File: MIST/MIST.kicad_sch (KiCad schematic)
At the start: 2 parts

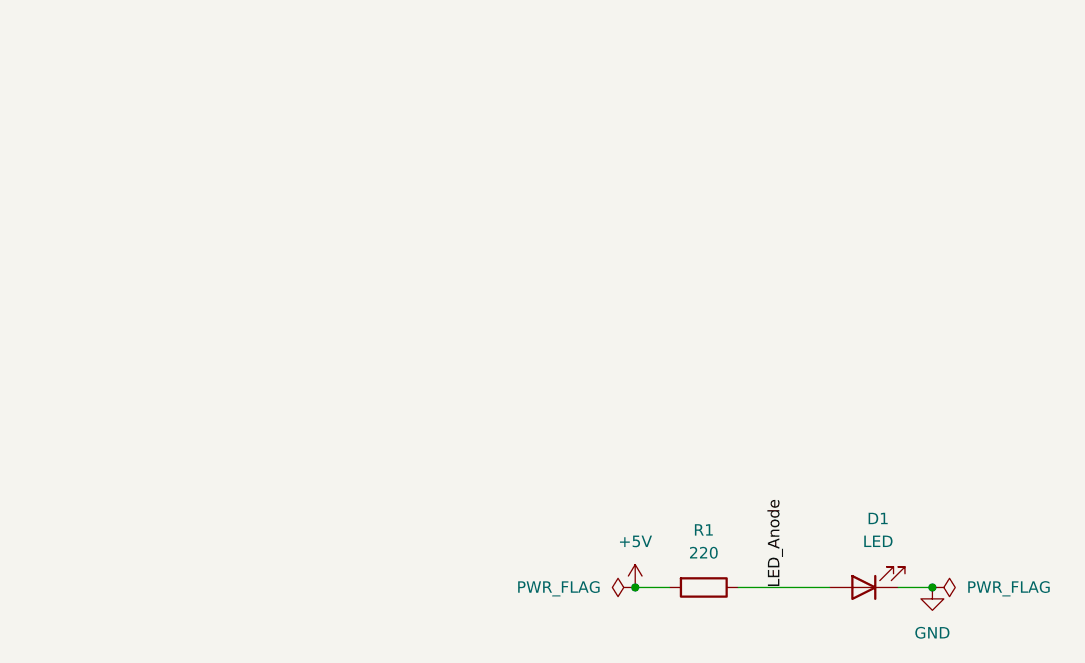
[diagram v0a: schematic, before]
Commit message: finished BOM and added resources and started layout
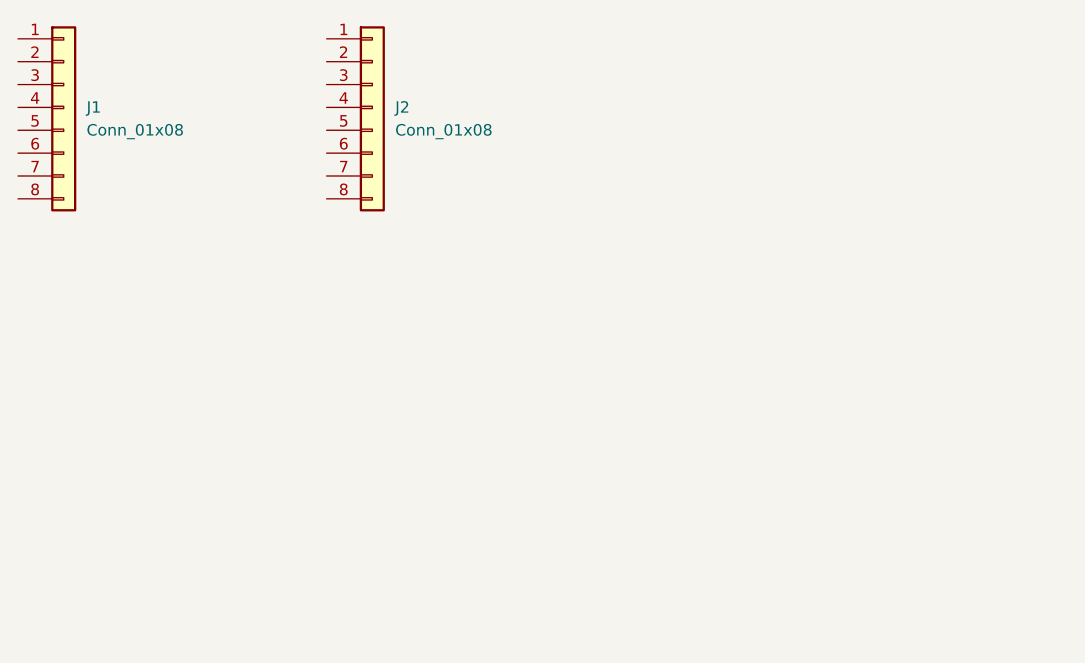
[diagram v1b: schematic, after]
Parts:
- removed D1: LED, LED_SMD:LED-APA102-2020, symbol Device:LED
- removed R1: 220, Resistor_SMD:R_0201_0603Metric, symbol Device:R
- added J1, J2: Conn_01x08, Connector_PinHeader_2.54mm:PinHeader_1x08_P2.54mm_Vertical, symbol Connector_Generic:Conn_01x08

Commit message: finished schematic. updated BOM. stuff.
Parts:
- added C1, C2: 100n, Capacitor_SMD:C_0805_2012Metric, symbol Device:C
- added C3, C4: 22pF, Capacitor_SMD:C_0805_2012Metric, symbol Device:C
- added C5: 22uF, Capacitor_SMD:C_0805_2012Metric, symbol Device:C
- added C6, C8, C9: 0.1u, symbol Device:C
- added C7: 0.1n, symbol Device:C
- added J3: USB_C_Receptacle_PowerOnly_6P, Connector_USB:USB_C_Receptacle_GCT_USB4125-xx-x_6P_TopMnt_Horizontal, symbol Connector:USB_C_Receptacle_PowerOnly_6P
- added J4: ICSP, Connector_PinHeader_2.54mm:PinHeader_2x03_P2.54mm_Vertical, symbol Connector_Generic:Conn_02x03_Odd_Even
- added MK1: CMC-5042PF-AC, CMC-5042PF-AC:CUI_CMC-5042PF-AC, symbol CMC-5042PF-AC:CMC-5042PF-AC
- added R1: 10k, Resistor_SMD:R_1206_3216Metric, symbol Device:R
- added R10: 100k, symbol Device:R
- added R2, R3: 10k, symbol Device:R
- added R4, R5: 5.1k, Resistor_SMD:R_1206_3216Metric, symbol Device:R
- added R6, R7: 2k, symbol Device:R
- added R8, R9: 1M, symbol Device:R
- added S1, S2: SKRPABE010, SKRPABE010:SW_SKRPABE010, symbol SKRPABE010:SKRPABE010
- added U1: ATmega328PB-A, Package_QFP:TQFP-32_7x7mm_P0.8mm, symbol MCU_Microchip_ATmega:ATmega328PB-A
- added U2: MAX7219, symbol Driver_LED:MAX7219
- added U3: MAX4466EXK, MAX4466EXK:SOT65P210X110-5N, symbol MAX4466EXK:MAX4466EXK
- added Y1: 16 Mhz Crystal, Crystal:Crystal_SMD_3225-4Pin_3.2x2.5mm, symbol Device:Crystal_GND24
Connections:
- net ROW1 (P9): now reaches J2.1 (Pin_1)
- net ROW1 (P9): now also U2.2 (DIG_0)
- net ROW2 (P14): now reaches J2.2 (Pin_2)
- net ROW2 (P14): now also U2.11 (DIG_1)
- net ROW3 (P8): now reaches J2.3 (Pin_3)
- net ROW3 (P8): now also U2.6 (DIG_2)
- net ROW4 (P12): now reaches J2.4 (Pin_4)
- net ROW4 (P12): now also U2.7 (DIG_3)
- net ROW5 (P1): now reaches J2.5 (Pin_5)
- net ROW5 (P1): now also U2.3 (DIG_4)
- net ROW6 (P7): now reaches J2.6 (Pin_6)
- net ROW6 (P7): now also U2.10 (DIG_5)
- net ROW7 (P2): now reaches J2.7 (Pin_7)
- net ROW7 (P2): now also U2.5 (DIG_6)
- net ROW8 (P5): now reaches J2.8 (Pin_8)
- net ROW8 (P5): now also U2.8 (DIG_7)
- net COL1 (P13): now reaches J1.1 (Pin_1)
- net COL1 (P13): now also U2.22 (SEG_DP)
- net COL2 (P3): now reaches J1.2 (Pin_2)
- net COL2 (P3): now also U2.14 (SEG_A)
- net COL3 (P4): now reaches J1.3 (Pin_3)
- net COL3 (P4): now also U2.16 (SEG_B)
- net COL4 (P10): now reaches J1.4 (Pin_4)
- net COL4 (P10): now also U2.20 (SEG_C)
- net COL5 (P6): now reaches J1.5 (Pin_5)
- net COL5 (P6): now also U2.23 (SEG_D)
- net COL6 (P11): now reaches J1.6 (Pin_6)
- net COL6 (P11): now also U2.21 (SEG_E)
- net COL7 (P15): now reaches J1.7 (Pin_7)
- net COL7 (P15): now also U2.15 (SEG_F)
- net COL8 (P16): now reaches J1.8 (Pin_8)
- net COL8 (P16): now also U2.17 (SEG_G)
- new net: C6.2, R6.2, R7.1
- new net: MK1.OUT, R7.2, R8.2, R9.1, U3.1 (IN+)
- new net: R3.1, U2.18 (ISET)
- new net: C7.1, R10.1, R2.1, U3.3 (IN-)
- new net !RESET: J4.5 (Pin_5), R1.1, S1.1, S1.2, U1.29 (~{RESET}/PC6)
- new net +5V: C1.2, C5.2, C8.1, C9.1, J3.A9 (VBUS), J3.B9 (VBUS), J4.2 (Pin_2), R1.2, R3.2, R6.1, R8.1, U1.18 (AVCC), U1.4 (VCC), U2.19 (V+), U3.5 (VCC)
- new net ADC0: C7.2, R10.2, U1.23 (PC0), U3.4 (OUT)
- new net AREF: C2.2, U1.20 (AREF)
- new net CC1: J3.A5 (CC1), R5.1
- new net CC2: J3.B5 (CC2), R4.1
- new net GND: C1.1, C2.1, C3.2, C4.1, C5.1, C6.1, C8.2, C9.2, J3.A12 (GND), J3.B12 (GND), J3.S1 (SHIELD), J4.6 (Pin_6), MK1.GND, R2.2, R4.2, R5.2, R9.2, S1.3, S1.4, S2.3, S2.4, U1.21 (GND), U1.5 (GND), U2.4 (GND), U2.9 (GND), U3.2 (GND), Y1.2, Y1.4
- new net MISO: J4.1 (Pin_1), U1.16 (PB4)
- new net MOSI: J4.4 (Pin_4), U1.15 (PB3), U2.1 (DIN)
- new net SCK: J4.3 (Pin_3), U1.17 (PB5), U2.13 (CLK)
- new net SS: U1.14 (PB2), U2.12 (LOAD)
- new net SWITCHMODE: S2.1, S2.2, U1.2 (PD4)
- new net XTAL1: C3.1, U1.7 (XTAL1/PB6), Y1.1
- new net XTAL2: C4.2, U1.8 (XTAL2/PB7), Y1.3
- no-connect marks 0 -> 19
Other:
- note added: "Bulk Capacitor"
- note added: "Crystal Oscillator"
- note added: "In-Circuit Serial Programming"
- note added: "LED Matrix"
- note added: "Microcontroller"
- note added: "Microphone"
- note added: "Reset Button"
- note added: "Switch Mode Button"
- note added: "USB Type-C - Power Only"
- moved on the sheet: J1, J2

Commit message: finished schematic and layout
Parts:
- C6, C7, C8, C9, R3: footprint (none) -> Capacitor_SMD:C_0805_2012Metric
- R10, R2, R6, R7, R8, R9: footprint (none) -> Resistor_SMD:R_0805_2012Metric
- R4, R5: footprint Resistor_SMD:R_1206_3216Metric -> Capacitor_SMD:C_0805_2012Metric
- U2: footprint (none) -> Package_SO:SOIC-24W_7.5x15.4mm_P1.27mm
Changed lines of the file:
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@@
 			)
 		)
-		(property "Footprint" ""
+		(property "Footprint" "Capacitor_SMD:C_0805_2012Metric"
 			(at 266.7 48.5648 0)
 			(effects
@@
 			)
 		)
-		(property "Footprint" "Resistor_SMD:R_1206_3216Metric"
+		(property "Footprint" "Capacitor_SMD:C_0805_2012Metric"
 			(at 87.122 166.37 90)
 			(effects
@@
 			)
 		)
-		(property "Footprint" ""
+		(property "Footprint" "Resistor_SMD:R_0805_2012Metric"
 			(at 289.052 55.88 90)
 			(effects
@@
 			)
 		)
-		(property "Footprint" ""
+		(property "Footprint" "Capacitor_SMD:C_0805_2012Metric"
 			(at 269.748 127 90)
 			(effects
@@
 			)
 		)
-		(property "Footprint" ""
+		(property "Footprint" "Package_SO:SOIC-24W_7.5x15.4mm_P1.27mm"
 			(at 281.94 149.86 0)
 			(effects
@@
 			)
 		)
-		(property "Footprint" "Resistor_SMD:R_1206_3216Metric"
+		(property "Footprint" "Capacitor_SMD:C_0805_2012Metric"
 			(at 97.282 166.37 90)
 			(effects
@@
 			)
 		)
-		(property "Footprint" ""
+		(property "Footprint" "Resistor_SMD:R_0805_2012Metric"
 			(at 337.82 94.488 90)
 			(effects
@@
 			)
 		)
-		(property "Footprint" ""
+		(property "Footprint" "Capacitor_SMD:C_0805_2012Metric"
 			(at 341.63 105.7148 0)
 			(effects
@@
 			)
 		)
-		(property "Footprint" ""
+		(property "Footprint" "Capacitor_SMD:C_0805_2012Metric"
 			(at 263.8552 151.13 0)
 			(effects
@@
 			)
 		)
-		(property "Footprint" ""
+		(property "Footprint" "Resistor_SMD:R_0805_2012Metric"
 			(at 273.812 55.88 90)
 			(effects
@@
 			)
 		)
-		(property "Footprint" ""
+		(property "Footprint" "Resistor_SMD:R_0805_2012Metric"
 			(at 289.052 78.74 90)
 			(effects
@@
 			)
 		)
-		(property "Footprint" ""
+		(property "Footprint" "Resistor_SMD:R_0805_2012Metric"
 			(at 273.812 43.18 90)
 			(effects
@@
 			)
 		)
-		(property "Footprint" ""
+		(property "Footprint" "Resistor_SMD:R_0805_2012Metric"
 			(at 303.022 78.74 90)
 			(effects
@@
 			)
 		)
-		(property "Footprint" ""
+		(property "Footprint" "Capacitor_SMD:C_0805_2012Metric"
 			(at 371.8052 46.99 0)
 			(effects

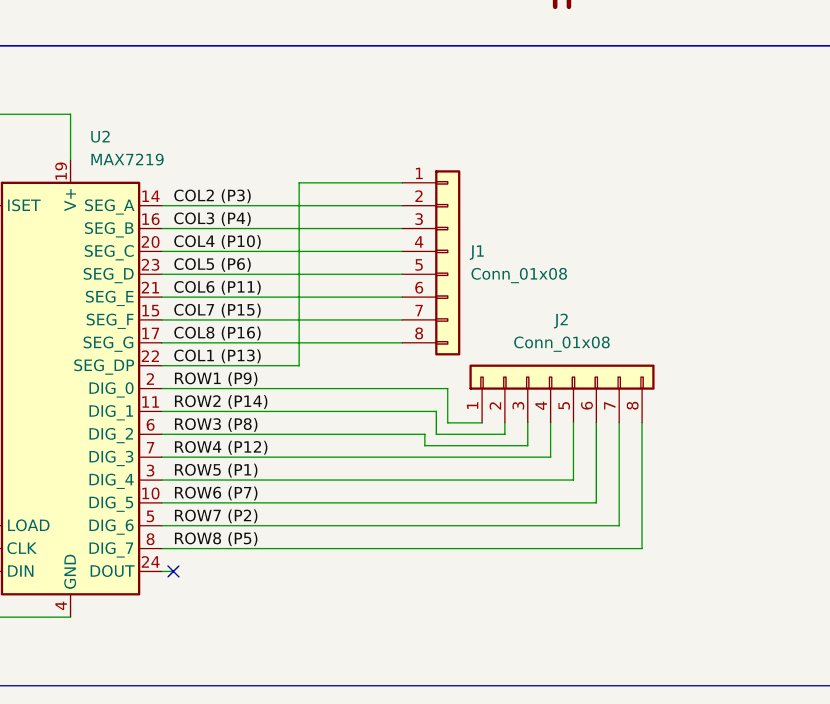
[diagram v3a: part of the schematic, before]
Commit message: fixed wrong matrix pin mappings schematic.
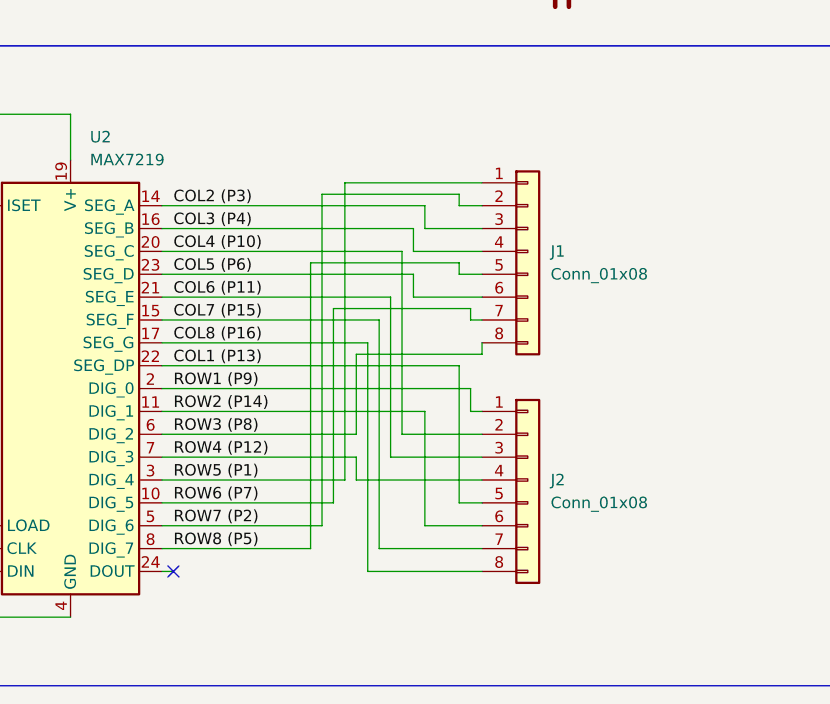
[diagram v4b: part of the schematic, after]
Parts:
- R1: footprint Resistor_SMD:R_1206_3216Metric -> Resistor_SMD:R_0805_2012Metric
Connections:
- net COL1 (P13): now also J2.5 (Pin_5); no longer J1.1 (Pin_1)
- net COL2 (P3): now also J1.3 (Pin_3); no longer J1.2 (Pin_2)
- net COL3 (P4): now also J1.4 (Pin_4); no longer J1.3 (Pin_3)
- net COL4 (P10): now also J2.2 (Pin_2); no longer J1.4 (Pin_4)
- net COL5 (P6): now also J1.6 (Pin_6); no longer J1.5 (Pin_5)
- net COL6 (P11): now also J2.3 (Pin_3); no longer J1.6 (Pin_6)
- net COL7 (P15): now also J2.7 (Pin_7); no longer J1.7 (Pin_7)
- net COL8 (P16): now also J2.8 (Pin_8); no longer J1.8 (Pin_8)
- net ROW2 (P14): now also J2.6 (Pin_6); no longer J2.2 (Pin_2)
- net ROW3 (P8): now also J1.8 (Pin_8); no longer J2.3 (Pin_3)
- net ROW5 (P1): now also J1.1 (Pin_1); no longer J2.5 (Pin_5)
- net ROW6 (P7): now also J1.7 (Pin_7); no longer J2.6 (Pin_6)
- net ROW7 (P2): now also J1.2 (Pin_2); no longer J2.7 (Pin_7)
- net ROW8 (P5): now also J1.5 (Pin_5); no longer J2.8 (Pin_8)
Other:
- moved on the sheet: J1, J2
